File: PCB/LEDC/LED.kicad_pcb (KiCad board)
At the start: 2 copper layers, 70 x 70 mm, 36 parts, among them J1 Reset, J2 Wago, J3 TC2030-USB-NL-DS, J5 USB-C-Socket-H, SW1 Button, U1 ICS43434_MEMS_Mic, U6 ESP32-S3-MINI-1, U7 MD8942

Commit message: Tidy
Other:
- board text removed: "led.revk.uk"

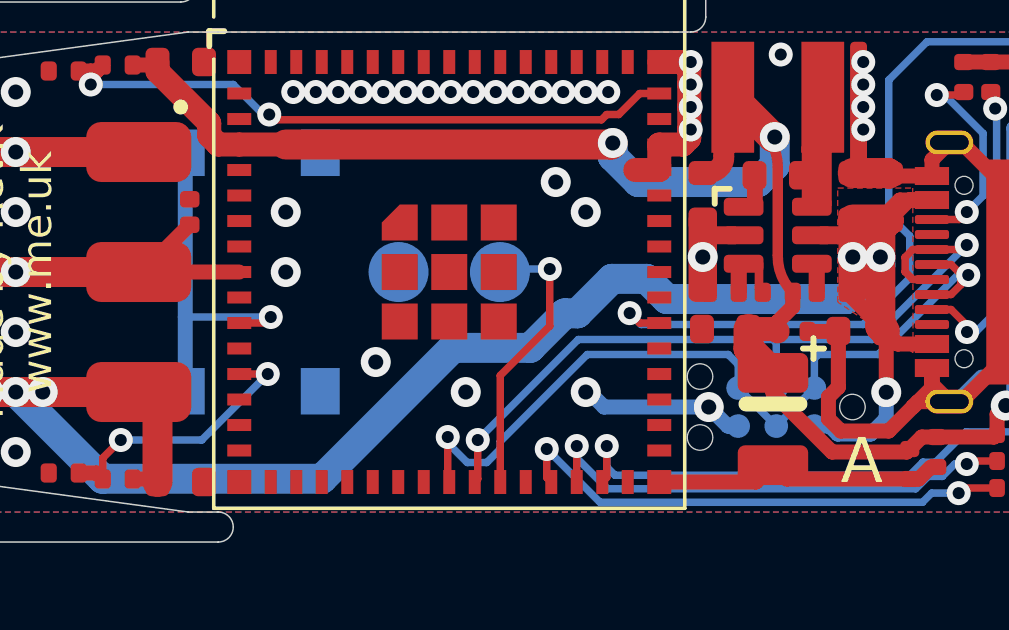
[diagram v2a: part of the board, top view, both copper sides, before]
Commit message: Larger caps
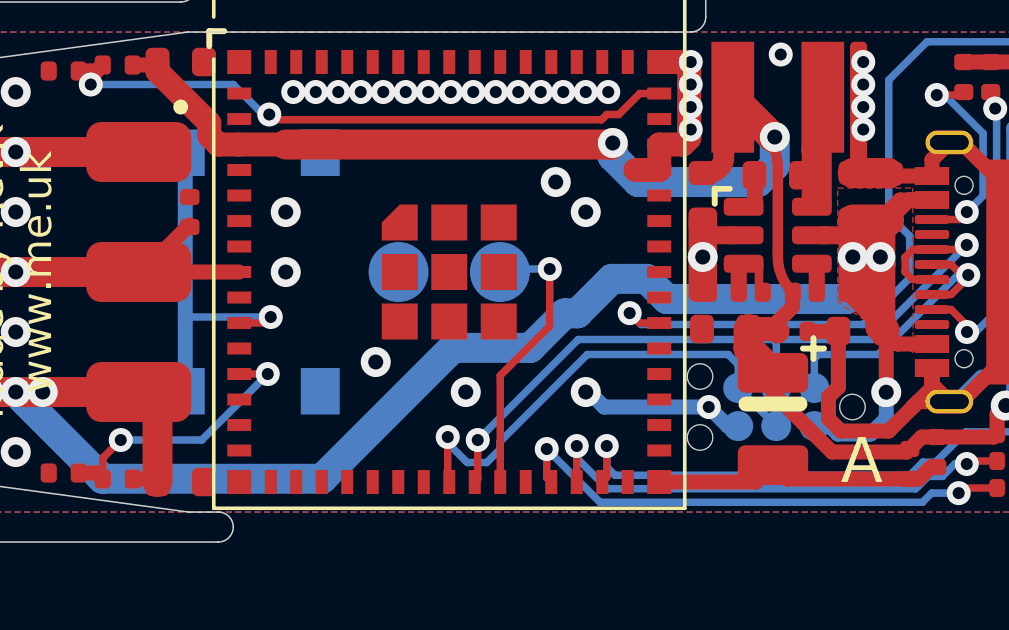
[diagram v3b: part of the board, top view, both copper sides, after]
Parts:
- C14, C5, C6, C7: value 10uF 35V -> 100uF 35V

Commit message: Bigger caps
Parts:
- removed C14: 100uF 35V, RevK:C_0603
- C5, C6, C7: value 100uF 35V -> 22uF 35V; footprint RevK:C_0603 -> RevK:C_0805
- moved R1 0.40 mm to (87.0, 106.9)
- moved R2 0.40 mm to (87.0, 93.1)
- moved C9 0.20 mm to (85.4, 93.3)
- moved R3 0.20 mm to (85.4, 106.7)
- moved C6 0.14 mm to (89.4, 106.9)
- moved C7 0.14 mm to (89.4, 93.1)
- moved C5 0.10 mm to (112.2, 102.0), turned to 180 degrees
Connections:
- C5 pad 1: GND -> DC
- C5 pad 2: DC -> GND
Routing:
- net GND: track 73.1 -> 78.7 mm
- net Net-(J5-CC2): track 6.99 -> 6.01 mm
- net DC: track 68.6 -> 69.5 mm
- net BLINK: track 25.2 -> 24.6 mm
- net Net-(U6-EN): track 21.1 -> 21.7 mm

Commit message: New design
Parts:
- added C14: 47uF, RevK:C_0603, F.Cu at (113.8, 106.5)
- added R7: 47R, RevK:R_0402, F.Cu at (112.8, 106.9)
- added U2: IRMHF384, RevK:IR-SMD-4P,3.35x3.9mm, F.Cu at (109.7, 105.3)
- C1: value 220uF Tant -> 220uF; footprint RevK:CP_EIA-3528-21_Kemet-B -> RevK:C_1206
- U1: footprint RevK:ICS43434_MEMS_Mic -> RevK:ICS43434_MEMS_Mic_Open
- moved C1 13.0 mm to (114.8, 93.2), turned to 180 degrees
- moved R6 2.33 mm to (113.6, 94.7), turned to 0 degrees
- moved C13 2.02 mm to (115.7, 105.7), turned to -90 degrees
- moved C4 1.39 mm to (118.2, 94.7), turned to 180 degrees
- moved R5 1.20 mm to (116.4, 94.7), turned to 0 degrees
- moved U1 0.82 mm to (118.8, 106.1)
- moved J3 0.50 mm to (109.4, 105.0)
- moved C8 0.32 mm to (114.8, 105.7), turned to -90 degrees
- moved C5 0.16 mm to (112.1, 102.0)
- moved C2 0.13 mm to (109.8, 101.9)
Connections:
- U6 pad 32: unconnected-(U6-GPIO36-Pad32) -> IR
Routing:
- net GND: track 78.7 -> 71.7 mm, vias 40 -> 37
- net IR: track 0.00 -> 4.05 mm
- net SCK: track 21.5 -> 18.5 mm
- net Net-(J1-Pin_2): track 9.34 -> 12.2 mm
- net +3V3: track 55.0 -> 52.6 mm, vias 4 -> 3
- net Net-(J5-CC1): track 10.3 -> 12.5 mm
- net Net-(U2-VCC): track 0.00 -> 2.15 mm
- net BLINK: track 24.6 -> 26.7 mm
- net DC: track 69.5 -> 68.4 mm
- net WS: track 17.1 -> 18.0 mm
- net SD: track 16.4 -> 17.3 mm
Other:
- board text added: "36"

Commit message: Tweak
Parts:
- moved U2 0.19 mm to (109.5, 105.2)
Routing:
- net GND: track 71.7 -> 68.0 mm
- net +3V3: track 52.6 -> 53.5 mm
- net Net-(U2-VCC): track 2.15 -> 2.99 mm

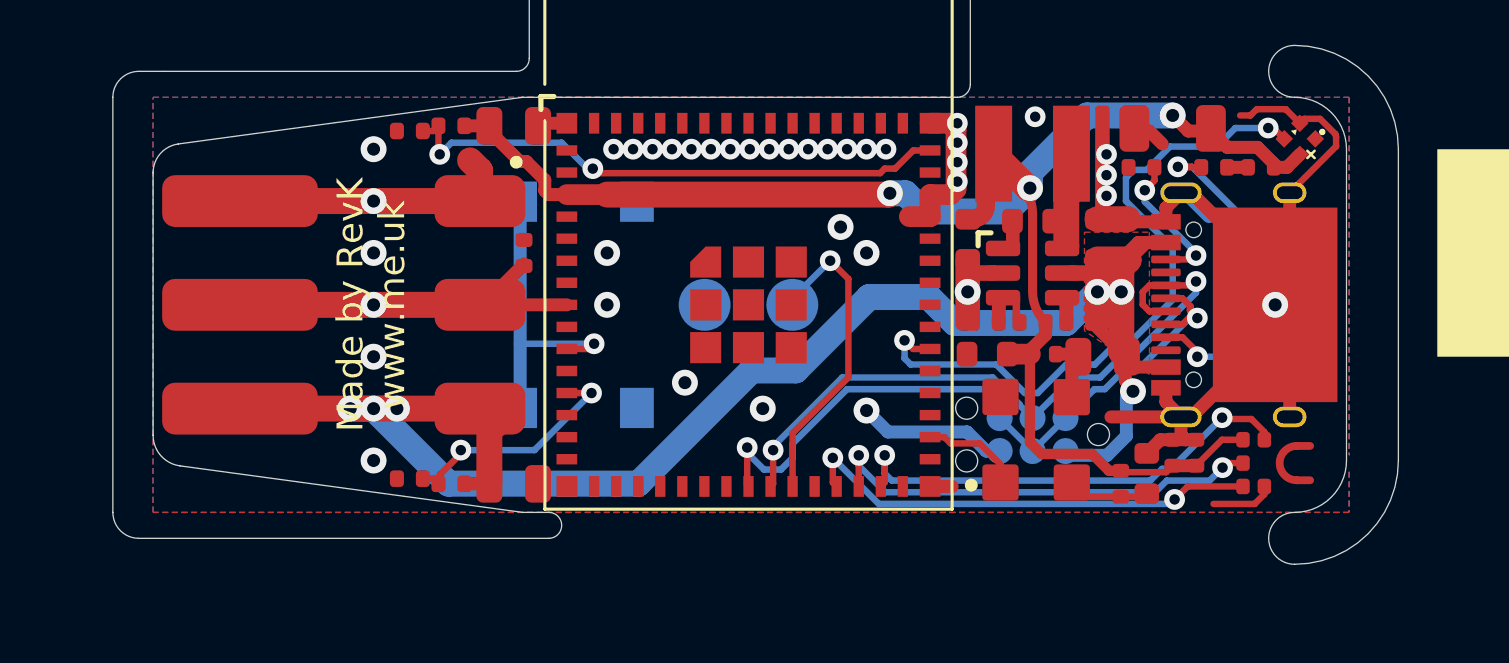
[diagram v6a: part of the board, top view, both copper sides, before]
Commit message: New power control on LEDC
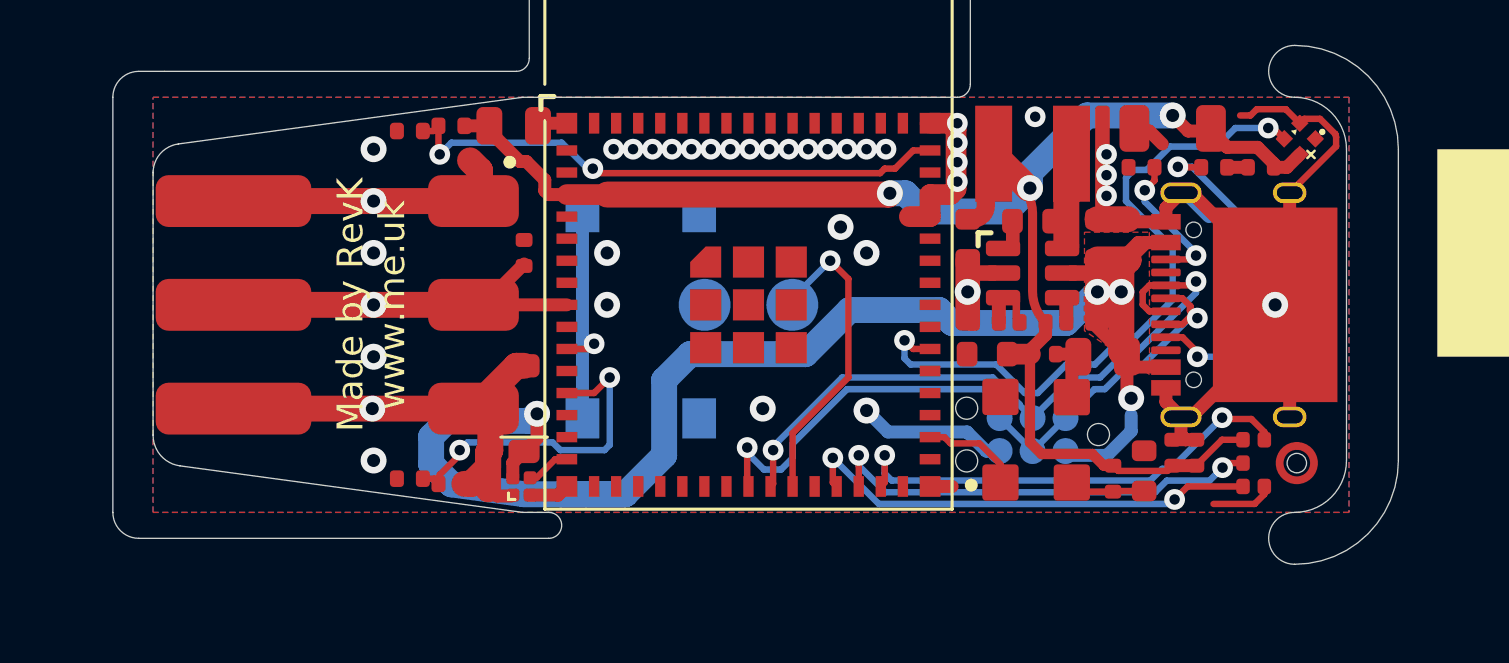
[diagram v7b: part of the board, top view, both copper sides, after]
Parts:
- removed C6: 22uF 35V, RevK:C_0805
- added D6: MBR0530, RevK:D_SOD-123, F.Cu at (89.8, 104.0)
- added U8: ~, RevK:WCSP-4-0.78x0.78, F.Cu at (89.7, 107.0)
- U1: footprint RevK:ICS43434_MEMS_Mic_Open -> RevK:ICS43434_MEMS_Mic
- moved SW1 2.43 mm to (94.3, 100.4)
- moved R7 0.36 mm to (112.5, 106.7)
- moved J2 0.25 mm to (83.2, 100.0)
- moved C14 0.14 mm to (113.7, 106.4)
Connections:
- J2 pad 3: DC -> LEDPWR
- R1 pad 1: DC -> LEDPWR
- U6 pad 15: unconnected-(U6-GPIO11-Pad15) -> PWR
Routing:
- net LEDPWR: track 0.00 -> 18.0 mm, vias 0 -> 1
- net DC: track 68.4 -> 61.4 mm, vias 6 -> 4
- net ADC: track 9.27 -> 13.0 mm
- net GND: track 68.0 -> 65.1 mm, vias 37 -> 36
- net PUSH: track 11.9 -> 9.53 mm
- net PWR: track 0.00 -> 1.71 mm
- net Net-(U2-VCC): track 2.99 -> 2.41 mm
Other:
- board text added: "(5V/2A WHEN USB)"
- board text added: "11"
- board text added: "PWR"
- board text removed: "(5V WHEN USB)"
- board text removed: "6x6 BTN"

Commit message: Revert as too high voltage for part
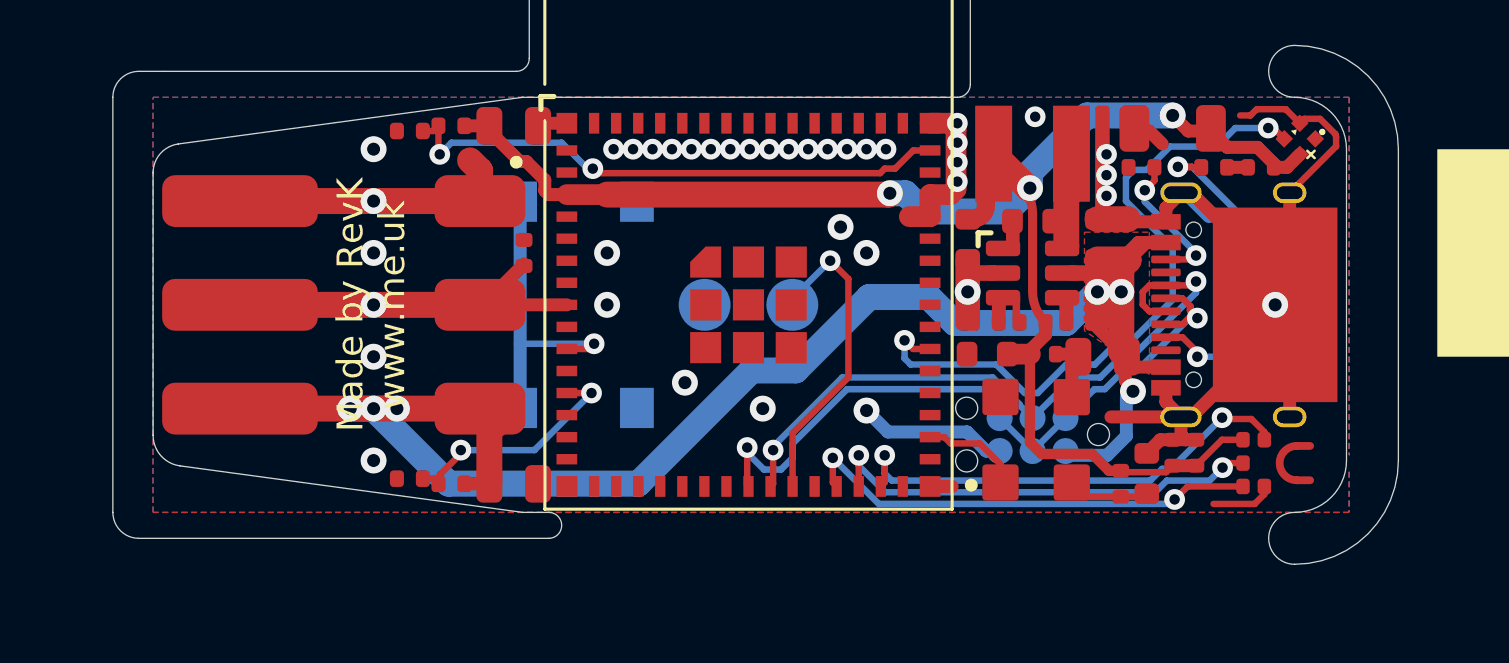
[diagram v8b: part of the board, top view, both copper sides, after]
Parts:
- removed D6: MBR0530, RevK:D_SOD-123
- removed U8: ~, RevK:WCSP-4-0.78x0.78
- added C6: 22uF 35V, RevK:C_0805, F.Cu at (89.4, 106.9)
- U1: footprint RevK:ICS43434_MEMS_Mic -> RevK:ICS43434_MEMS_Mic_Open
- moved SW1 2.43 mm to (91.9, 100.0)
- moved R7 0.36 mm to (112.8, 106.9)
- moved J2 0.25 mm to (83.5, 100.0)
- moved C14 0.14 mm to (113.8, 106.5)
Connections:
- J2 pad 3: LEDPWR -> DC
- R1 pad 1: LEDPWR -> DC
- U6 pad 15: PWR -> unconnected-(U6-GPIO11-Pad15)
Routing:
- net LEDPWR: track 18.0 -> 0.00 mm, vias 1 -> 0
- net DC: track 61.4 -> 68.4 mm, vias 4 -> 6
- net ADC: track 13.0 -> 9.27 mm
- net GND: track 65.1 -> 68.0 mm, vias 36 -> 37
- net PUSH: track 9.53 -> 11.9 mm
- net PWR: track 1.71 -> 0.00 mm
- net Net-(U2-VCC): track 2.41 -> 2.99 mm
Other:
- board text added: "(5V WHEN USB)"
- board text added: "6x6 BTN"
- board text removed: "(5V/2A WHEN USB)"
- board text removed: "11"
- board text removed: "PWR"
